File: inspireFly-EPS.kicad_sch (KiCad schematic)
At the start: 98 parts, among them J1 USB4085-GF-A_REVB, J2 Conn_01x02_Pin, Q10 SQJA62EP-T1_GE3, Q3 SQJA62EP-T1_GE3, Q4 SQJA62EP-T1_GE3, Q5 SQJA62EP-T1_GE3, Q6 SQJA62EP-T1_GE3, Q7 SQJA62EP-T1_GE3, Q8 SQJA62EP-T1_GE3, Q9 SQJA62EP-T1_GE3, U1 STM32U575RIT6, U2 BQ25750RRVR, U3 TCAN332DCNR, U4 MAX77504AAFC+T, U5 INA180A3IDBVT, U6 INA180A3IDBVT, U7 INA180A3IDBVT, U8 TPS63070RNMR, U9 TPS63070RNMR

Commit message: Routing fixes
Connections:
- net I2C3-SCL: now also U2.1 (SCL); no longer U2.2 (SDA)
- net I2C3-SDA: now also U2.2 (SDA); no longer U2.1 (SCL)
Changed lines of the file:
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@@
 	(wire
 		(pts
+			(xy 109.22 341.63) (xy 118.11 341.63)
+		)
+		(stroke
+			(width 0)
+			(type default)
+		)
+	)
+	(wire
+		(pts
 			(xy 44.45 245.11) (xy 46.99 245.11)
 		)
@@
 	(wire
 		(pts
-			(xy 109.22 341.63) (xy 118.11 341.63)
-		)
-		(stroke
-			(width 0)
-			(type default)
-		)
-	)
-	(wire
-		(pts
 			(xy 459.74 290.83) (xy 459.74 294.64)
 		)
@@
 	(wire
 		(pts
-			(xy 386.08 234.95) (xy 396.24 234.95)
+			(xy 109.22 339.09) (xy 118.11 339.09)
 		)
 		(stroke
@@
 	(wire
 		(pts
-			(xy 170.18 35.56) (xy 170.18 39.37)
+			(xy 386.08 234.95) (xy 396.24 234.95)
 		)
 		(stroke
@@
 	(wire
 		(pts
-			(xy 85.09 342.9) (xy 77.47 342.9)
+			(xy 170.18 35.56) (xy 170.18 39.37)
 		)
 		(stroke
@@
 	(wire
 		(pts
-			(xy 69.85 342.9) (xy 64.77 342.9)
+			(xy 85.09 342.9) (xy 77.47 342.9)
 		)
 		(stroke
@@
 	(wire
 		(pts
-			(xy 321.31 220.98) (xy 327.66 220.98)
+			(xy 69.85 342.9) (xy 64.77 342.9)
 		)
 		(stroke
@@
 	(wire
 		(pts
-			(xy 173.99 382.27) (xy 203.2 382.27)
+			(xy 321.31 220.98) (xy 327.66 220.98)
 		)
 		(stroke
@@
 	(wire
 		(pts
-			(xy 271.78 224.79) (xy 271.78 222.25)
+			(xy 173.99 382.27) (xy 203.2 382.27)
 		)
 		(stroke
@@
 	(wire
 		(pts
-			(xy 256.54 347.98) (xy 264.16 347.98)
+			(xy 271.78 224.79) (xy 271.78 222.25)
 		)
 		(stroke
@@
 	(wire
 		(pts
-			(xy 109.22 339.09) (xy 118.11 339.09)
+			(xy 256.54 347.98) (xy 264.16 347.98)
 		)
 		(stroke
@@
 	(global_label "I2C3-SCL"
 		(shape input)
-		(at 109.22 341.63 180)
+		(at 109.22 339.09 180)
 		(fields_autoplaced yes)
 		(effects
@@
 		)
 		(property "Intersheetrefs" "${INTERSHEET_REFS}"
-			(at 96.861 341.63 0)
+			(at 96.861 339.09 0)
 			(effects
 				(font
@@
 	(global_label "I2C3-SDA"
 		(shape input)
-		(at 109.22 339.09 180)
+		(at 109.22 341.63 180)
 		(fields_autoplaced yes)
 		(effects
@@
 		)
 		(property "Intersheetrefs" "${INTERSHEET_REFS}"
-			(at 96.8005 339.09 0)
+			(at 96.8005 341.63 0)
 			(effects
 				(font

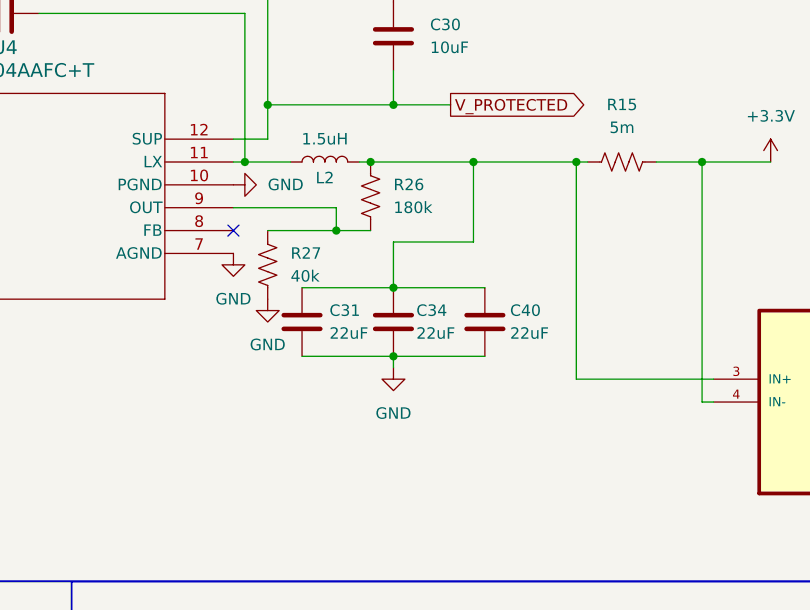
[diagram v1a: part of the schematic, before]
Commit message: Fixed mistake on 3.3V reg
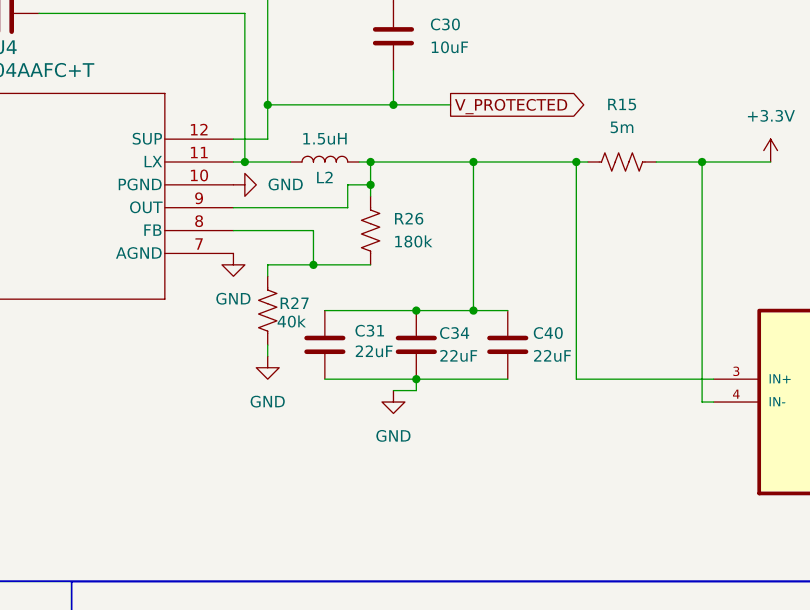
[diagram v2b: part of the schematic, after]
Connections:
- net at C31.2, C34.2, C40.2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: now also U4.9 (OUT)
- net at R26.1, R27.2: now also U4.8 (FB); no longer U4.9 (OUT)
- no-connect marks 12 -> 11
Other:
- moved on the sheet: C31, C34, C40, R26, R27

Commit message: Lots of routing
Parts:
- removed C14: 47uF, inspireFly-EPS-footprints:CAP_EEEFN1J470L, symbol Device:C
- removed C25, C26: 100nF, Capacitor_SMD:C_0402_1005Metric_Pad0.74x0.62mm_HandSolder, symbol Device:C
- removed R17: 10, Resistor_SMD:R_0603_1608Metric_Pad0.98x0.95mm_HandSolder, symbol Device:R_US
- removed U5: INA180A3IDBVT, inspireFly-EPS-footprints:SOT95P280X145-5N, symbol InspireFly-EPS-sym_lib:INA180A3IDBVT
- added C35, C36, C47, C48, C49, C50: 22uF, Capacitor_SMD:C_0805_2012Metric_Pad1.18x1.45mm_HandSolder, symbol Device:C
- added C44, C45: 10uF, Capacitor_SMD:C_0805_2012Metric_Pad1.18x1.45mm_HandSolder, symbol Device:C
- added C46: 100nF, Capacitor_SMD:C_0805_2012Metric_Pad1.18x1.45mm_HandSolder, symbol Device:C
- added JP1: BAT_ENABLE, Jumper:SolderJumper-2_P1.3mm_Open_RoundedPad1.0x1.5mm, symbol Jumper:SolderJumper_2_Open
- added L4: 2.2uH, symbol Device:L
- added Q1: SQJ123ELP-T1_GE3, inspireFly-EPS-footprints:TRANS_SQJA62EP-T1_GE3, symbol Simulation_SPICE:PMOS
- added R30: 40k, Resistor_SMD:R_0402_1005Metric_Pad0.72x0.64mm_HandSolder, symbol Device:R_US
- added R31: 210k, Resistor_SMD:R_0402_1005Metric_Pad0.72x0.64mm_HandSolder, symbol Device:R_US
- added R32: 200k, Resistor_SMD:R_0402_1005Metric_Pad0.72x0.64mm_HandSolder, symbol Device:R_US
- C30, C31, C34, C37, C38, C40, C41, C42, C43: footprint (none) -> Capacitor_SMD:C_0805_2012Metric_Pad1.18x1.45mm_HandSolder
- C32, C33: footprint (none) -> Capacitor_SMD:C_0402_1005Metric_Pad0.74x0.62mm_HandSolder
- C39: footprint Capacitor_SMD:C_0805_2012Metric_Pad1.18x1.45mm_HandSolder -> Capacitor_SMD:C_0402_1005Metric_Pad0.74x0.62mm_HandSolder
- R15: value 5m -> 47k; footprint Resistor_SMD:R_1206_3216Metric_Pad1.30x1.75mm_HandSolder -> Resistor_SMD:R_0603_1608Metric_Pad0.98x0.95mm_HandSolder
- R25, R26, R27, R28, R29: footprint (none) -> Resistor_SMD:R_0402_1005Metric_Pad0.72x0.64mm_HandSolder
- U4: footprint 21-100406_F122A2F+2_MXM -> inspireFly-EPS-footprints:21-100406_F122A2F&plus_2_MXM
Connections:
- net +3.3V: now also C31.2, C34.2, C40.2, L2.2, R26.2, U4.9 (OUT); no longer R15.2
- net +5V: now also C41.2, C42.2, C43.2
- net ADC1_IN3: now also C29.1, R24.2
- net BAT +: now also R15.1, Q1.3 (S); no longer R5.2, R7.2, R8.1
- net GND: now also C17.1, U9.10 (PGND), U9.15 (VSEL), U9.4 (GND), U9.6 (FB2), C35.2, C36.2, C44.2, C45.2, C46.2, C47.1, C48.1, C49.1, C50.2, JP1.2 (B), R30.2; no longer C17.2
- net V_PROTECTED: now also C17.2, U9.1 (PS/SYNC), U9.12_13 (VIN), C44.1
- net at Q10.3 (S), Q7.1 (D), R5.1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: now also C35.1, C36.1, C50.1; no longer C17.1
- net at C38.1, R16.1, R29.1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: no longer C41.2, C42.2, C43.2
- net at U9.11 (L1): now also L4.1
- net SUPER_CAP_CHARGE_ENABLE: now reaches U9.14 (EN)
- net at U9.3 (VAUX): now also C46.1
- net at U9.5 (FB): now also R30.1, R31.2
- net +9V: now reaches U9.7_8 (VOUT)
- net +9V: now also C45.1, C47.2, C48.2, C49.2, R32.2
- net at U9.9 (L2): now also L4.2
- removed net ADC1_IN5: C29.1, R24.2, U1.14 (PA0)
- new net: Q1.1 (D), R5.2, R7.2, R8.1
- new net: JP1.1 (A), Q1.2 (G), R15.2
- new net: R31.1, R32.1
- no-connect marks 11 -> 12
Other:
- moved on the sheet: C17, C41, C42, C43

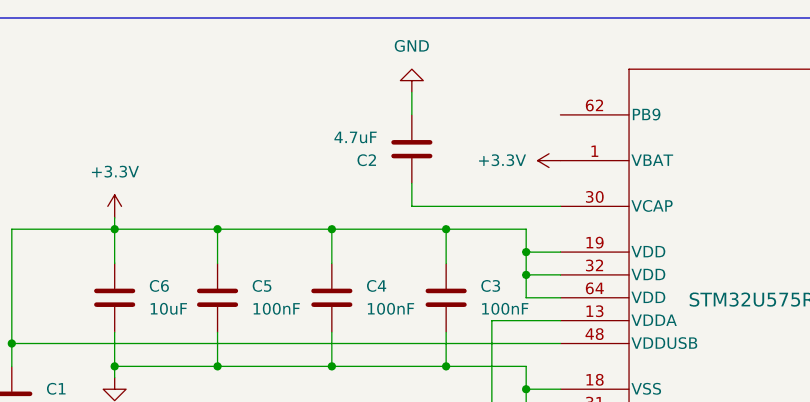
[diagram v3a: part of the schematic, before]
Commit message: Updated STM location
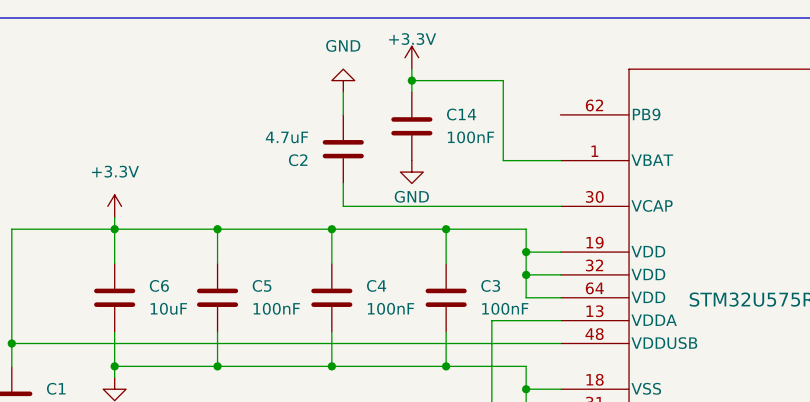
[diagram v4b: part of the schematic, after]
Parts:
- added C14: 100nF, Capacitor_SMD:C_0402_1005Metric_Pad0.74x0.62mm_HandSolder, symbol Device:C
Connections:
- net +3.3V: now also C14.1
- net GND: now also C14.2
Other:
- moved on the sheet: C2
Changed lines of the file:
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@@
 	)
 	(junction
+		(at 203.2 19.05)
+		(diameter 0)
+		(color 0 0 0 0)
+	)
+	(junction
 		(at 44.45 237.49)
 		(diameter 0)
@@
 	(wire
 		(pts
+			(xy 213.36 27.94) (xy 213.36 19.05)
+		)
+		(stroke
+			(width 0)
+			(type default)
+		)
+	)
+	(wire
+		(pts
 			(xy 299.72 55.88) (xy 295.91 55.88)
 		)
@@
 	(wire
 		(pts
-			(xy 203.2 30.48) (xy 203.2 33.02)
+			(xy 195.58 30.48) (xy 195.58 33.02)
 		)
 		(stroke
@@
 	(wire
 		(pts
+			(xy 203.2 17.78) (xy 203.2 19.05)
+		)
+		(stroke
+			(width 0)
+			(type default)
+		)
+	)
+	(wire
+		(pts
 			(xy 190.5 55.88) (xy 195.58 55.88)
 		)
@@
 	(wire
 		(pts
-			(xy 203.2 33.02) (xy 219.71 33.02)
+			(xy 195.58 33.02) (xy 219.71 33.02)
 		)
 		(stroke
@@
 	(wire
 		(pts
-			(xy 203.2 20.32) (xy 203.2 22.86)
+			(xy 195.58 20.32) (xy 195.58 22.86)
 		)
 		(stroke
@@
 	(wire
 		(pts
+			(xy 213.36 19.05) (xy 203.2 19.05)
+		)
+		(stroke
+			(width 0)
+			(type default)
+		)
+	)
+	(wire
+		(pts
 			(xy 240.03 356.87) (xy 240.03 359.41)
 		)
@@
 	(wire
 		(pts
+			(xy 219.71 27.94) (xy 213.36 27.94)
+		)
+		(stroke
+			(width 0)
+			(type default)
+		)
+	)
+	(wire
+		(pts
 			(xy 99.06 393.7) (xy 104.14 393.7)
 		)
@@
 	(wire
 		(pts
+			(xy 203.2 19.05) (xy 203.2 20.32)
+		)
+		(stroke
+			(width 0)
+			(type default)
+		)
+	)
+	(wire
+		(pts
 			(xy 44.45 191.77) (xy 46.99 191.77)
 		)
@@
 	(symbol
 		(lib_id "power:GND")
+		(at 203.2 27.94 0)
+		(unit 1)
+		(exclude_from_sim no)
+		(in_bom yes)
+		(on_board yes)
+		(dnp no)
+		(property "Reference" "#PWR042"
+			(at 203.2 34.29 0)
+			(effects
+				(font
+					(size 1.27 1.27)
+				)
+				(hide yes)
+			)
+		)
+		(property "Value" "GND"
+			(at 203.2 32.004 0)
+			(effects
+				(font
+					(size 1.27 1.27)
+				)
+			)
+		)
+		(property "Footprint" ""
+			(at 203.2 27.94 0)
+			(effects
+				(font
+					(size 1.27 1.27)
+				)
+				(hide yes)
+			)
+		)
+		(property "Datasheet" ""
+			(at 203.2 27.94 0)
+			(effects
+				(font
+					(size 1.27 1.27)
+				)
+				(hide yes)
+			)
+		)
+		(property "Description" "Power symbol creates a global label with name \"GND\" , ground"
+			(at 203.2 27.94 0)
+			(effects
+				(font
+					(size 1.27 1.27)
+				)
+				(hide yes)
+			)
+		)
+		(pin "1"
+		)
+		(instances
+			(project "inspireFly-EPS"
+				(path "/85d7bd69-2813-405d-9eae-82e9bb551a95"
+					(reference "#PWR042")
+					(unit 1)
+				)
+			)
+		)
+	)
+	(symbol
+		(lib_id "power:GND")
 		(at 113.03 354.33 270)
 		(unit 1)
@@
 	(symbol
 		(lib_id "power:GND")
-		(at 203.2 20.32 180)
+		(at 195.58 20.32 180)
 		(unit 1)
 		(exclude_from_sim no)
@@
 		(fields_autoplaced yes)
 		(property "Reference" "#PWR03"
-			(at 203.2 13.97 0)
+			(at 195.58 13.97 0)
 			(effects
 				(font
@@
 		)
 		(property "Value" "GND"
-			(at 203.2 15.24 0)
+			(at 195.58 15.24 0)
 			(effects
 				(font
@@
 		)
 		(property "Footprint" ""
-			(at 203.2 20.32 0)
+			(at 195.58 20.32 0)
 			(effects
 				(font
@@
 		)
 		(property "Datasheet" ""
-			(at 203.2 20.32 0)
+			(at 195.58 20.32 0)
 			(effects
 				(font
@@
 		)
 		(property "Description" "Power symbol creates a global label with name \"GND\" , ground"
-			(at 203.2 20.32 0)
+			(at 195.58 20.32 0)
 			(effects
 				(font
@@
 	(symbol
 		(lib_id "power:+3.3V")
-		(at 219.71 27.94 90)
+		(at 203.2 17.78 0)
 		(unit 1)
 		(exclude_from_sim no)
@@
 		(on_board yes)
 		(dnp no)
-		(fields_autoplaced yes)
 		(property "Reference" "#PWR01"
-			(at 223.52 27.94 0)
+			(at 203.2 21.59 0)
 			(effects
 				(font
@@
 		)
 		(property "Value" "+3.3V"
-			(at 215.9 27.9399 90)
+			(at 203.2 14.478 0)
 			(effects
 				(font
 					(size 1.27 1.27)
 				)
-				(justify left)
 			)
 		)
 		(property "Footprint" ""
-			(at 219.71 27.94 0)
+			(at 203.2 17.78 0)
 			(effects
 				(font
@@
 		)
 		(property "Datasheet" ""
-			(at 219.71 27.94 0)
+			(at 203.2 17.78 0)
 			(effects
 				(font
@@
 		)
 		(property "Description" "Power symbol creates a global label with name \"+3.3V\""
-			(at 219.71 27.94 0)
+			(at 203.2 17.78 0)
 			(effects
 				(font
@@
 	(symbol
 		(lib_id "Device:C")
-		(at 203.2 26.67 180)
+		(at 195.58 26.67 180)
 		(unit 1)
 		(exclude_from_sim no)
@@
 		(fields_autoplaced yes)
 		(property "Reference" "C2"
-			(at 199.39 27.9401 0)
+			(at 191.77 27.9401 0)
 			(effects
 				(font
@@
 		)
 		(property "Value" "4.7uF"
-			(at 199.39 25.4001 0)
+			(at 191.77 25.4001 0)
 			(effects
 				(font
@@
 		)
 		(property "Footprint" "Capacitor_SMD:C_0402_1005Metric_Pad0.74x0.62mm_HandSolder"
-			(at 202.2348 22.86 0)
+			(at 194.6148 22.86 0)
 			(effects
 				(font
@@
 		)
 		(property "Datasheet" "~"
-			(at 203.2 26.67 0)
+			(at 195.58 26.67 0)
 			(effects
 				(font
@@
 		)
 		(property "Description" "Unpolarized capacitor"
-			(at 203.2 26.67 0)
+			(at 195.58 26.67 0)
 			(effects
 				(font
@@
 					(unit 1)
 				)
+			)
+		)
+	)
+	(symbol
+		(lib_id "Device:C")
+		(at 203.2 24.13 0)
+		(unit 1)
+		(exclude_from_sim no)
+		(in_bom yes)
+		(on_board yes)
+		(dnp no)
+		(fields_autoplaced yes)
+		(property "Reference" "C14"
+			(at 207.01 22.8599 0)
+			(effects
+				(font
+					(size 1.27 1.27)
+				)
+				(justify left)
+			)
+		)
+		(property "Value" "100nF"
+			(at 207.01 25.3999 0)
+			(effects
+				(font
+					(size 1.27 1.27)
+				)
+				(justify left)
+			)
+		)
+		(property "Footprint" "Capacitor_SMD:C_0402_1005Metric_Pad0.74x0.62mm_HandSolder"
+			(at 204.1652 27.94 0)
+			(effects
+				(font
+					(size 1.27 1.27)
+				)
+				(hide yes)
+			)
+		)
+		(property "Datasheet" "~"
+			(at 203.2 24.13 0)
+			(effects
+				(font
+					(size 1.27 1.27)
+				)
+				(hide yes)
+			)
+		)
+		(property "Description" "Unpolarized capacitor"
+			(at 203.2 24.13 0)
+			(effects
+				(font
+					(size 1.27 1.27)
+				)
+				(hide yes)
+			)
+		)
+		(pin "1"
+		)
+		(pin "2"
+		)
+		(instances
+			(project "inspireFly-EPS"
+				(path "/85d7bd69-2813-405d-9eae-82e9bb551a95"
+					(reference "C14")
+					(unit 1)
+				)

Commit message: Added Dead battery to BQ and other routing changes
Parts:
- removed R10: 5.24k, Resistor_SMD:R_0402_1005Metric_Pad0.72x0.64mm_HandSolder, symbol Device:R_US
- removed R11: 30.31k, Resistor_SMD:R_0402_1005Metric_Pad0.72x0.64mm_HandSolder, symbol Device:R_US
- removed TH1: Thermistor_US, symbol Device:Thermistor_US
- added D4, D5: DFLS130L-7, inspireFly-EPS-footprints:DFLS130L7, symbol Device:D_Schottky
- added R33, R34: 10K, Resistor_SMD:R_0402_1005Metric_Pad0.72x0.64mm_HandSolder, symbol Device:R_US
- added TP1: DRV_SUP, TestPoint:TestPoint_Pad_D1.5mm, symbol Connector:TestPoint
- added TP2: V_PROTECTED, TestPoint:TestPoint_Pad_D1.5mm, symbol Connector:TestPoint
- added TP3: +5V, TestPoint:TestPoint_Pad_D1.5mm, symbol Connector:TestPoint
- added TP4: +3V, TestPoint:TestPoint_Pad_D1.5mm, symbol Connector:TestPoint
- added TP5: V_BAT, TestPoint:TestPoint_Pad_D1.5mm, symbol Connector:TestPoint
- added TP6: V_COMBINED, TestPoint:TestPoint_Pad_D1.5mm, symbol Connector:TestPoint
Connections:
- net +3.3V: now also TP4.1
- net +5V: now also D4.2 (A), TP3.1; no longer C22.2, U2.23 (DRV_SUP)
- net GND: now also R34.2; no longer U2.8 (TS)
- net REGEN: now also D5.2 (A), R33.1
- net V_BUS_COMBINED: now also TP6.1
- net V_PROTECTED: now also TP2.1
- net at Q1.1 (D), R5.2, R7.2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: now also TP5.1
- new net: C22.2, D4.1 (K), D5.1 (K), TP1.1, U2.23 (DRV_SUP)
- new net: R33.2, R34.1, U2.8 (TS)
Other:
- moved on the sheet: C22

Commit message: About ready for proto 1
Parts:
- removed C17: 47uF, inspireFly-EPS-footprints:CAP_EEEFN1J470L, symbol Device:C
- added C17: 47uF, inspireFly-EPS-footprints:CAP_EEEFN1J470L, symbol Device:C_Polarized
- added C25: 100nF, Capacitor_SMD:C_0402_1005Metric_Pad0.74x0.62mm_HandSolder, symbol Device:C
- added C26, C51: 10pF, Capacitor_SMD:C_0402_1005Metric_Pad0.74x0.62mm_HandSolder, symbol Device:C
- added R35, R36: 10K, Resistor_SMD:R_0402_1005Metric_Pad0.72x0.64mm_HandSolder, symbol Device:R_US
- added SW1, SW2: SW_Push, inspireFly-EPS-footprints:SW_PTS810_SJM_250_SMTR_LFS, symbol Switch:SW_Push
- added TP7: +9V, TestPoint:TestPoint_Pad_D1.5mm, symbol Connector:TestPoint
- added Y1: Crystal_GND2, inspireFly-EPS-footprints:XTAL_TSX-3225_16.0000MF18X-AC0, symbol Device:Crystal_GND2
- C46: footprint Capacitor_SMD:C_0805_2012Metric_Pad1.18x1.45mm_HandSolder -> Capacitor_SMD:C_0402_1005Metric_Pad0.74x0.62mm_HandSolder
- L4: footprint (none) -> inspireFly-EPS-footprints:WE-MXGI_4020
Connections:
- net SUPER_CAP_CHARGE_ENABLE is gone; now on net V_PROTECTED: U9.14 (EN)
- net +3.3V: now also R36.2, SW1.1
- net +9V: now also TP7.1
- net GND: now also C17.2, C26.1, C51.1, R35.2, SW2.1, Y1.2
- net V_PROTECTED: now also C17.1
- net at U1.4 (PC15-OSC32_OUT): now also C26.2, Y1.1
- net PH0-OSC-IN: now reaches U1.5 (PH0-OSC_IN)
- net PH0-OSC-IN: now also C51.2, Y1.3
- net at U1.60 (PH3-BOOT0): now also R35.1, SW1.2
- net at U1.7 (NRST): now also C25.1, R36.1
- new net: C25.2, SW2.2
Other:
- moved on the sheet: C1, U1A

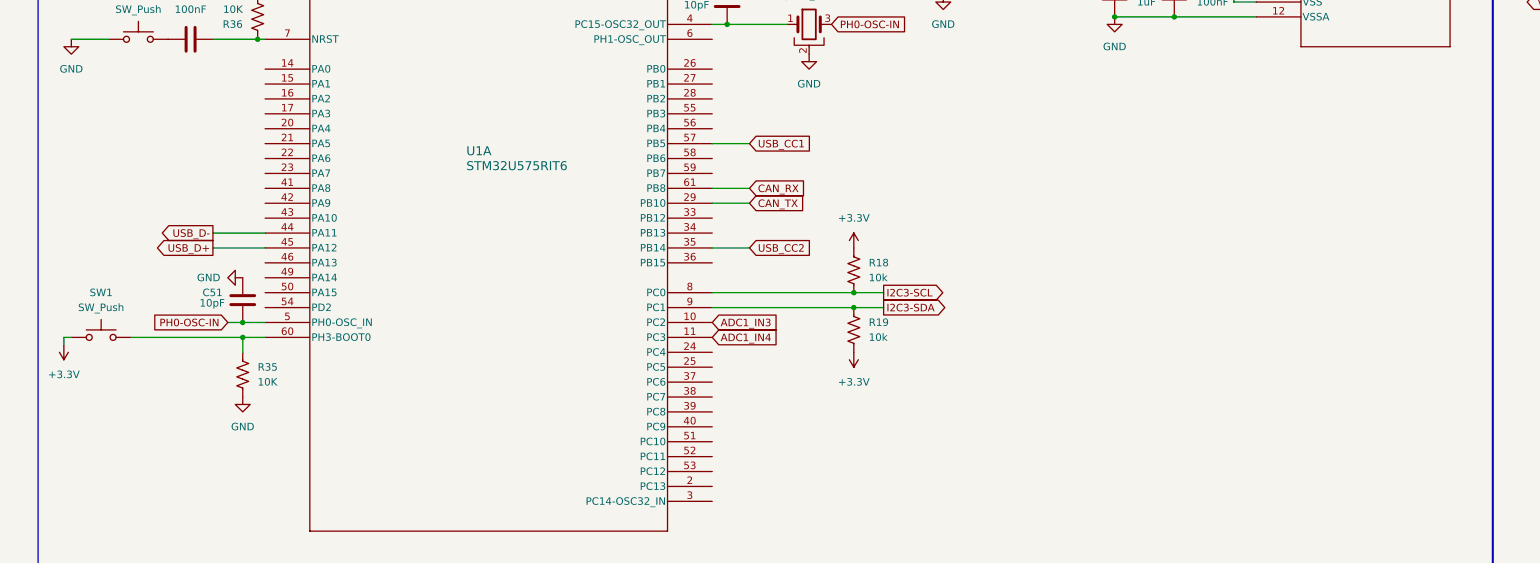
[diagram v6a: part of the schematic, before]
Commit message: Updated the ST575 to have a 14 pin debugger
Routed and added to schematic.
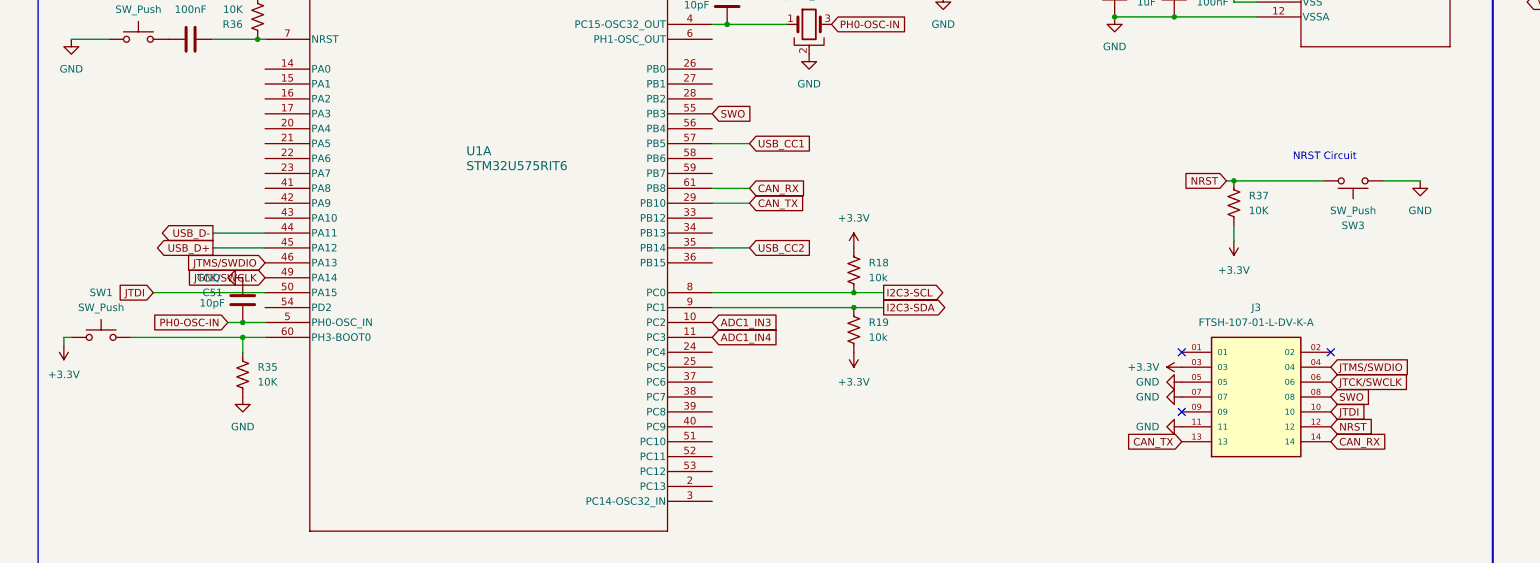
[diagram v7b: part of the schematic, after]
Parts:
- added J3: FTSH-107-01-L-DV-K-A, inspireFly-EPS-footprints:SAMTEC_FTSH-107-01-L-DV-K-A, symbol inspirefly:FTSH-107-01-L-DV-K-A
- added R37: 10K, Resistor_SMD:R_0402_1005Metric_Pad0.72x0.64mm_HandSolder, symbol Device:R_US
- added SW3: SW_Push, inspireFly-EPS-footprints:SW_PTS810_SJM_250_SMTR_LFS, symbol Switch:SW_Push
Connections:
- net +3.3V: now also J3.03, R37.2
- net CAN_RX: now also J3.14
- net CAN_TX: now also J3.13
- net GND: now also J3.05, J3.07, J3.11, SW3.1
- net JTMS/SWDIO: now reaches U1.46 (PA13)
- net JTMS/SWDIO: now also J3.04
- net JTCK/SWCLK: now reaches U1.49 (PA14)
- net JTCK/SWCLK: now also J3.06
- net JTDI: now reaches U1.50 (PA15)
- net JTDI: now also J3.10
- net SWO: now reaches U1.55 (PB3)
- net SWO: now also J3.08
- new net NRST: J3.12, R37.1, SW3.2
- no-connect marks 12 -> 15
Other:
- note added: "NRST Circuit"
